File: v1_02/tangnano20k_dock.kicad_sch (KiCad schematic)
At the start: 49 parts, among them J1 Mini-DIN-6, J12 Cliff DC10A, J14 Mini-DIN-6, J18 Conn_02x04_Odd_Even, J2 2x20 Pin Female, J3 Conn_01x03_Male, J4 Conn_01x20, J5 Conn_01x02, J6 RCA, J7 FCR684205T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

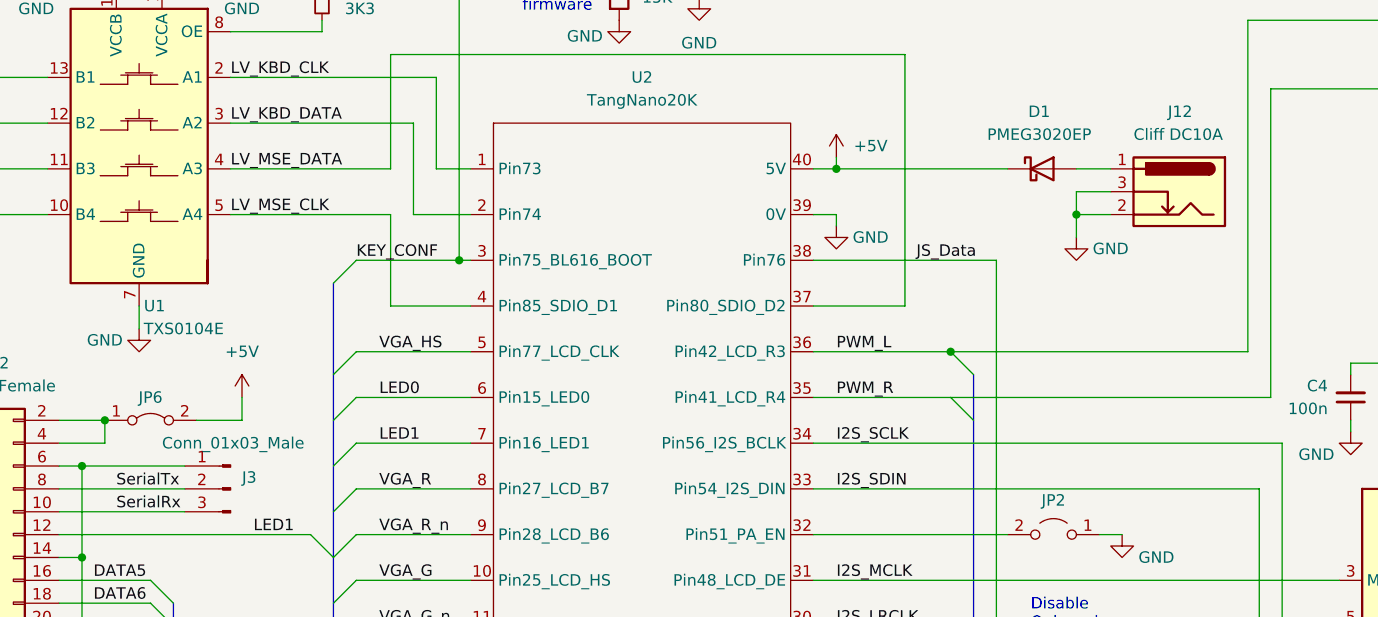
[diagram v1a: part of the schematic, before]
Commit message: v1_02: Updated symbols/footprints for KiCAD9; fix all ERC/DRC warnings
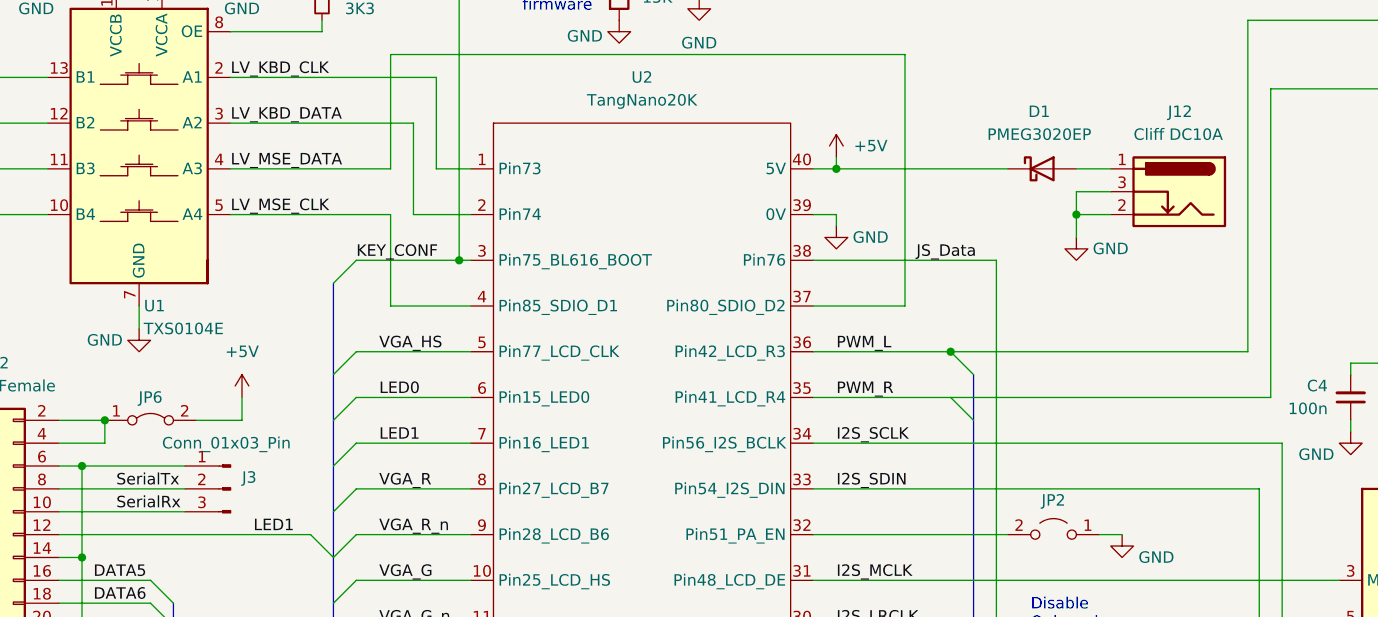
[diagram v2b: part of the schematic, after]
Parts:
- J3: value Conn_01x03_Male -> Conn_01x03_Pin; symbol Connector:Conn_01x03_Male -> Connector:Conn_01x03_Pin
- J8: symbol Connector:AudioJack3 -> Connector_Audio:AudioJack3
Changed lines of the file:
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@@
 			)
 		)
-		(property "Description" ""
+		(property "Description" "Resistor, small symbol"
 			(at 106.68 25.4 0)
 			(effects
@@
 			)
 		)
-		(property "Description" ""
+		(property "Description" "Power symbol creates a global label with name \"GND\" , ground"
 			(at 195.58 85.09 0)
 			(effects
@@
 			)
 		)
-		(property "Description" ""
+		(property "Description" "Power symbol creates a global label with name \"+5V\""
 			(at 22.86 52.07 0)
 			(effects
@@
 			)
 		)
-		(property "Description" ""
+		(property "Description" "Resistor, small symbol"
 			(at 232.41 35.56 0)
 			(effects
@@
 			)
 		)
-		(property "Description" ""
+		(property "Description" "Power symbol creates a global label with name \"GND\" , ground"
 			(at 97.79 21.59 0)
 			(effects
@@
 			)
 		)
-		(property "Description" ""
+		(property "Description" "Resistor, small symbol"
 			(at 166.37 130.81 0)
 			(effects
@@
 			)
 		)
-		(property "Description" ""
+		(property "Description" "Power symbol creates a global label with name \"GND\" , ground"
 			(at 232.41 120.65 0)
 			(effects
@@
 			)
 		)
-		(property "Description" ""
+		(property "Description" "Power symbol creates a global label with name \"GND\" , ground"
 			(at 22.86 82.55 0)
 			(effects
@@
 			)
 		)
-		(property "Description" ""
+		(property "Description" "Power symbol creates a global label with name \"GND\" , ground"
 			(at 120.65 142.24 0)
 			(effects
@@
 			)
 		)
-		(property "Description" ""
+		(property "Description" "Power symbol creates a global label with name \"GND\" , ground"
 			(at 22.86 31.75 0)
 			(effects
@@
 			)
 		)
-		(property "Description" ""
+		(property "Description" "Power symbol creates a global label with name \"+5V\""
 			(at 234.95 64.77 0)
 			(effects
@@
 			)
 		)
-		(property "Description" ""
+		(property "Description" "Resistor, small symbol"
 			(at 227.33 152.4 0)
 			(effects
@@
 			)
 		)
-		(property "Description" ""
+		(property "Description" "Power symbol creates a global label with name \"+3.3V\""
 			(at 118.11 138.43 0)
 			(effects
@@
 			)
 		)
-		(property "Description" ""
+		(property "Description" "Power symbol creates a global label with name \"+5V\""
 			(at 38.1 52.07 0)
 			(effects
@@
 			)
 		)
-		(property "Description" ""
+		(property "Description" "Power symbol creates a global label with name \"GND\" , ground"
 			(at 80.01 121.92 0)
 			(effects
@@
 	)
 	(symbol
-		(lib_id "Connector:AudioJack3")
+		(lib_id "Connector_Audio:AudioJack3")
 		(at 275.59 44.45 180)
 		(unit 1)
@@
 			)
 		)
-		(property "Description" ""
+		(property "Description" "Audio Jack, 3 Poles (Stereo / TRS)"
 			(at 275.59 44.45 0)
 			(effects
@@
 			)
 		)
-		(property "Description" ""
+		(property "Description" "Power symbol creates a global label with name \"GND\" , ground"
 			(at 250.19 160.02 0)
 			(effects
@@
 			)
 		)
-		(property "Description" ""
+		(property "Description" "Resistor, small symbol"
 			(at 50.8 24.13 0)
 			(effects
@@
 			)
 		)
-		(property "Description" ""
+		(property "Description" "Power symbol creates a global label with name \"+5V\""
 			(at 83.82 21.59 0)
 			(effects
@@
 			)
 		)
-		(property "Description" ""
+		(property "Description" "Power symbol creates a global label with name \"GND\" , ground"
 			(at 190.5 52.07 0)
 			(effects
@@
 			)
 		)
-		(property "Description" ""
+		(property "Description" "DC Barrel Jack with an internal switch"
 			(at 201.93 46.99 0)
 			(effects
@@
 			)
 		)
-		(property "Description" ""
+		(property "Description" "Power symbol creates a global label with name \"GND\" , ground"
 			(at 250.19 74.93 0)
 			(effects
@@
 			)
 		)
-		(property "Description" ""
+		(property "Description" "Power symbol creates a global label with name \"+5V\""
 			(at 97.79 69.85 0)
 			(effects
@@
 			)
 		)
-		(property "Description" ""
+		(property "Description" "Resistor, small symbol"
 			(at 50.8 59.69 0)
 			(effects
@@
 			)
 		)
-		(property "Description" ""
+		(property "Description" "Power symbol creates a global label with name \"GND\" , ground"
 			(at 262.89 30.48 0)
 			(effects
@@
 			)
 		)
-		(property "Description" ""
+		(property "Description" "Resistor, small symbol"
 			(at 232.41 156.21 0)
 			(effects
@@
 	)
 	(symbol
-		(lib_id "Connector:Conn_01x03_Male")
+		(lib_id "Connector:Conn_01x03_Pin")
 		(at 96.52 80.01 0)
 		(mirror y)
@@
 			)
 		)
-		(property "Value" "Conn_01x03_Male"
+		(property "Value" "Conn_01x03_Pin"
 			(at 88.9 74.93 0)
 			(effects
@@
 			)
 		)
-		(property "Description" ""
+		(property "Description" "Generic connector, single row, 01x03, script generated"
 			(at 96.52 80.01 0)
 			(effects
@@
 			)
 		)
-		(property "Description" ""
+		(property "Description" "Power symbol creates a global label with name \"GND\" , ground"
 			(at 173.99 143.51 0)
 			(effects
@@
 			)
 		)
-		(property "Description" ""
+		(property "Description" "Power symbol creates a global label with name \"+5V\""
 			(at 163.83 43.18 0)
 			(effects
@@
 			)
 		)
-		(property "Description" ""
+		(property "Description" "Power symbol creates a global label with name \"GND\" , ground"
 			(at 262.89 52.07 0)
 			(effects
@@
 			)
 		)
-		(property "Description" ""
+		(property "Description" "Power symbol creates a global label with name \"GND\" , ground"
 			(at 139.7 27.94 0)
 			(effects
@@
 			)
 		)
-		(property "Description" ""
+		(property "Description" "Power symbol creates a global label with name \"+3.3V\""
 			(at 35.56 74.93 0)
 			(effects
@@
 			)
 		)
-		(property "Description" ""
+		(property "Description" "Power symbol creates a global label with name \"GND\" , ground"
 			(at 38.1 31.75 0)
 			(effects
@@
 			)
 		)
-		(property "Description" ""
+		(property "Description" "Resistor, small symbol"
 			(at 270.51 77.47 0)
 			(effects
@@
 			)
 		)
-		(property "Description" ""
+		(property "Description" "Resistor, small symbol"
 			(at 50.8 52.07 0)
 			(effects
@@
 			)
 		)
-		(property "Description" ""
+		(property "Description" "Power symbol creates a global label with name \"GND\" , ground"
 			(at 255.27 114.3 0)
 			(effects
@@
 			)
 		)
-		(property "Description" ""
+		(property "Description" "Power symbol creates a global label with name \"+3.3V\""
 			(at 229.87 64.77 0)
 			(effects
@@
 			)
 		)
-		(property "Description" ""
+		(property "Description" "Power symbol creates a global label with name \"GND\" , ground"
 			(at 163.83 50.8 0)
 			(effects
@@
 			)
 		)
-		(property "Description" ""
+		(property "Description" "Power symbol creates a global label with name \"GND\" , ground"
 			(at 62.23 121.92 0)
 			(effects
@@
 			)
 		)
-		(property "Description" ""
+		(property "Description" "Power symbol creates a global label with name \"GND\" , ground"
 			(at 148.59 25.4 0)
 			(effects
@@
 			)
 		)
-		(property "Description" ""
+		(property "Description" "Power symbol creates a global label with name \"GND\" , ground"
 			(at 86.36 62.23 0)
 			(effects
@@
 			)
 		)
-		(property "Description" ""
+		(property "Description" "Resistor, small symbol"
 			(at 232.41 27.94 0)
 			(effects
@@
 			)
 		)
-		(property "Description" ""
+		(property "Description" "Power symbol creates a global label with name \"+5V\""
 			(at 22.86 74.93 0)
 			(effects
@@
 			)
 		)
-		(property "Description" ""
+		(property "Description" "Power symbol creates a global label with name \"GND\" , ground"
 			(at 74.93 21.59 0)
 			(effects
@@
 			)
 		)
-		(property "Description" ""
+		(property "Description" "Power symbol creates a global label with name \"GND\" , ground"
 			(at 91.44 189.23 0)
 			(effects
@@
 			)
 		)
-		(property "Description" ""
+		(property "Description" "Power symbol creates a global label with name \"GND\" , ground"
 			(at 77.47 142.24 0)
 			(effects
@@
 			)
 		)
-		(property "Description" ""
+		(property "Description" "Power symbol creates a global label with name \"GND\" , ground"
 			(at 232.41 160.02 0)
 			(effects
@@
 			)
 		)
-		(property "Description" ""
+		(property "Description" "Resistor, small symbol"
 			(at 50.8 31.75 0)
 			(effects
@@
 			)
 		)
-		(property "Description" ""
+		(property "Description" "Power symbol creates a global label with name \"+3.3V\""
 			(at 267.97 123.19 0)
 			(effects
@@
 			)
 		)
-		(property "Description" ""
+		(property "Description" "Power symbol creates a global label with name \"GND\" , ground"
 			(at 267.97 146.05 0)
 			(effects
@@
 			)
 		)
-		(property "Description" ""
+		(property "Description" "Power symbol creates a global label with name \"GND\" , ground"
 			(at 165.1 116.84 0)
 			(effects
@@
 			)
 		)
-		(property "Description" ""
+		(property "Description" "Power symbol creates a global label with name \"+3.3V\""
 			(at 172.72 116.84 0)
 			(effects
@@
 			)
 		)
-		(property "Description" ""
+		(property "Description" "Resistor, small symbol"
 			(at 262.89 77.47 0)
 			(effects
@@
 			)
 		)
-		(property "Description" ""
+		(property "Description" "Power symbol creates a global label with name \"+3.3V\""
 			(at 88.9 21.59 0)
 			(effects
@@
 			)
 		)
-		(property "Description" ""
+		(property "Description" "Power symbol creates a global label with name \"GND\" , ground"
 			(at 220.98 73.66 0)
 			(effects
@@
 			)
 		)
-		(property "Description" ""
+		(property "Description" "Power symbol creates a global label with name \"GND\" , ground"
 			(at 255.27 83.82 0)
 			(effects
@@
 			)
 		)
-		(property "Description" ""
+		(property "Description" "coaxial connector (BNC, SMA, SMB, SMC, Cinch/RCA, LEMO, ...)"
 			(at 250.19 152.4 0)
 			(effects
@@
 			)
 		)
-		(property "Description" ""
+		(property "Description" "Power symbol creates a global label with name \"GND\" , ground"
 			(at 270.51 52.07 0)
 			(effects
